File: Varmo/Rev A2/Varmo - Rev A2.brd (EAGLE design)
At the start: 131 x 87 mm, 88 parts, among them J1 22-05-7028-02, J2 22-05-7028-02, J3 22-05-7038-03, J4 22-05-7038-03, J5 22-05-7038-03, J6 22-05-7038-03, J7 22-05-7028-02, J8 22-05-7028-02, J9 22-05-7038-03, T1 MMBT2222AL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

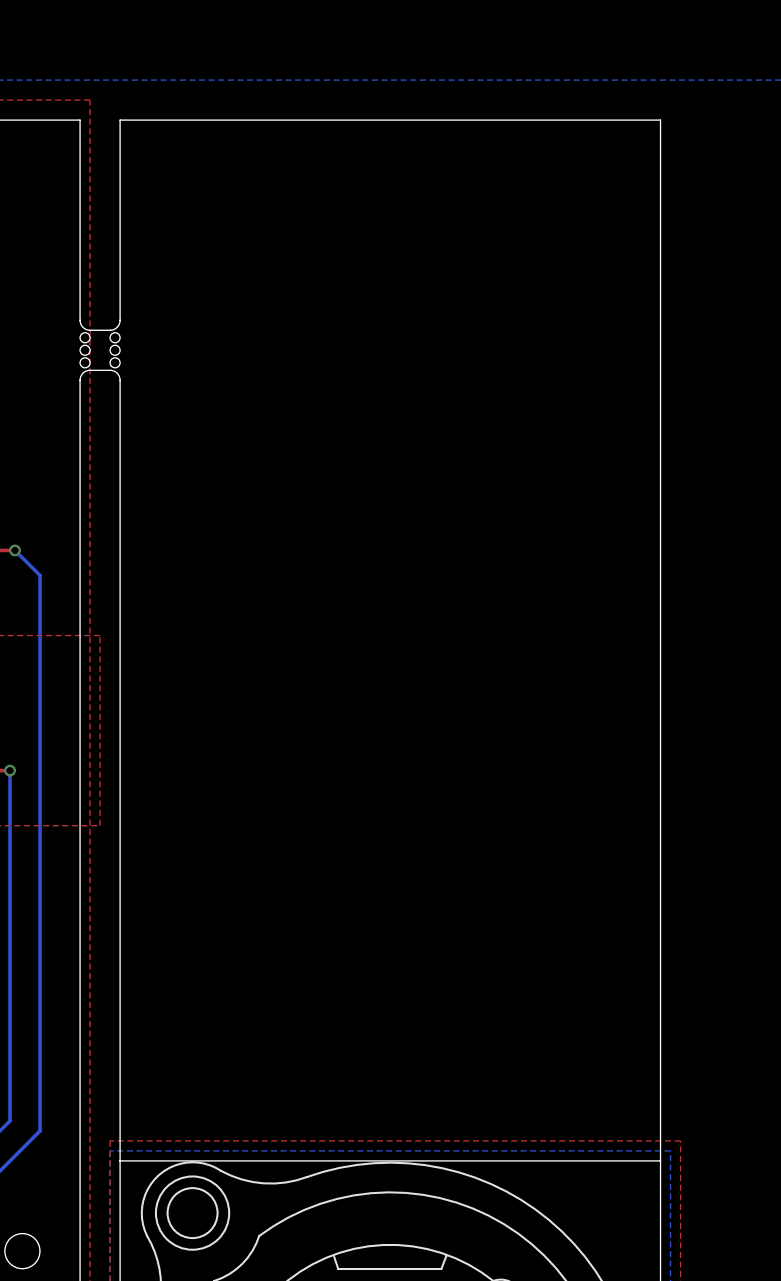
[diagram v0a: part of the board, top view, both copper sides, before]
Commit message: Add joystick to the board varmo rev a2
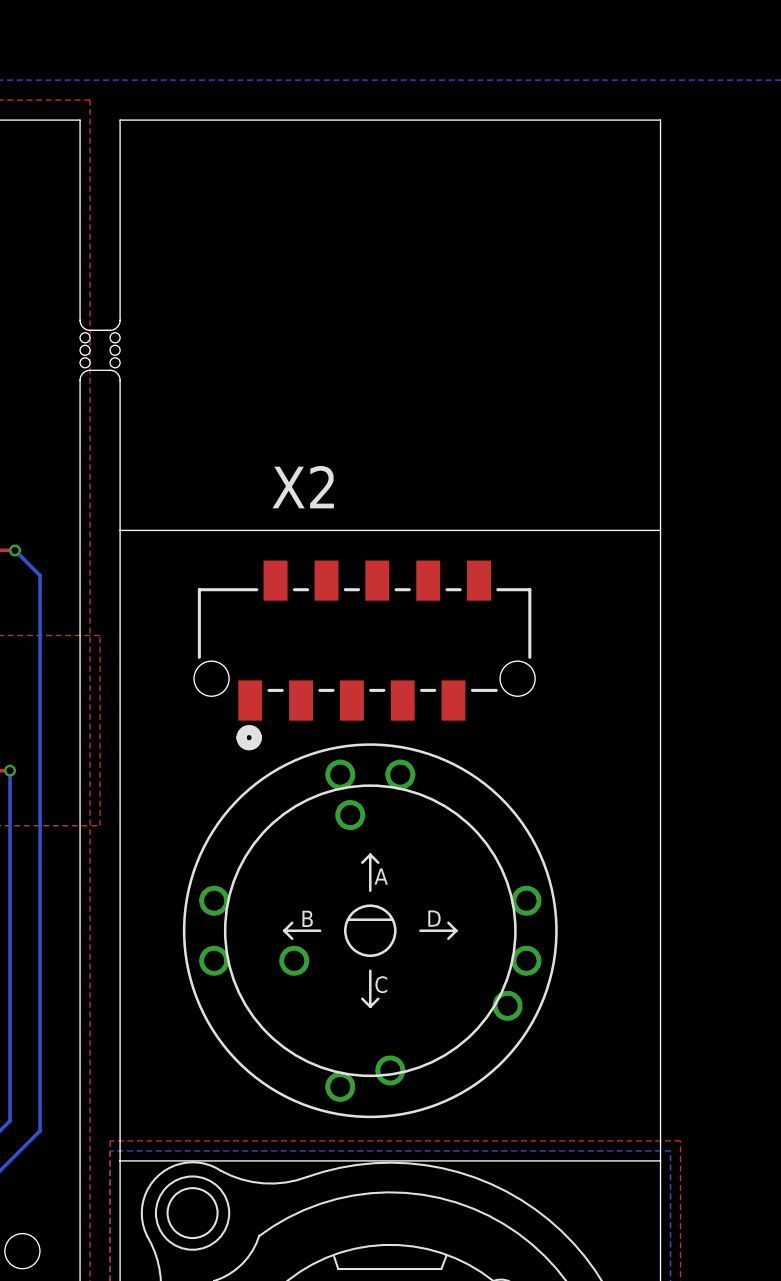
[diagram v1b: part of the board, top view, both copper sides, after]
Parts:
- added ENC1: RKJXTF42001, encoder:RKJXT1F
- added X2: 90814-0210, Molex_By_element14_Batch_1:MOLEX_90814-0210
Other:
- outline, holes or cut-outs redrawn
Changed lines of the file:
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@@
 <hole x="102.25" y="10.125" drill="0.5"/>
 <wire x1="104" y1="11" x2="104" y2="35" width="0" layer="20"/>
-<wire x1="104" y1="35" x2="104" y2="74" width="0" layer="20"/>
+<wire x1="104" y1="35" x2="104" y2="66.5" width="0" layer="20"/>
+<wire x1="104" y1="66.5" x2="104" y2="74" width="0" layer="20"/>
 <wire x1="104" y1="74" x2="103.5" y2="74.5" width="0" layer="20" curve="90"/>
 <wire x1="103.5" y1="74.5" x2="102.5" y2="74.5" width="0" layer="20"/>
@@
 <hole x="102.25" y="27" drill="0.5"/>
 <hole x="102.25" y="27.625" drill="0.5"/>
-<wire x1="131" y1="35" x2="131" y2="87" width="0" layer="20"/>
+<wire x1="131" y1="35" x2="131" y2="66.5" width="0" layer="20"/>
+<wire x1="131" y1="66.5" x2="131" y2="87" width="0" layer="20"/>
+<wire x1="104" y1="66.5" x2="131" y2="66.5" width="0" layer="20"/>
 </plain>
 <attributes>
@@
 </element>
 <element name="U$1" library="cc-by-sa" package="CC-BY-NC-SA" value="CC-BY-NC-SA" x="51.5" y="32.5" rot="R270"/>
+<element name="ENC1" library="encoder" package="RKJXT1F" value="RKJXTF42001" x="116.5" y="46.5"/>
+<element name="X2" library="Molex_By_element14_Batch_1" package="MOLEX_90814-0210" value="90814-0210" x="110.5" y="58">
+<attribute name="MF" value="" x="110.5" y="58" size="1.778" layer="27" display="off"/>
+<attribute name="OC_NEWARK" value="34R6217" x="110.5" y="58" size="1.778" layer="27" display="off"/>
+<attribute name="PACKAGE" value="CONN-10POS" x="110.5" y="58" size="1.778" layer="27" display="off"/>
+<attribute name="MPN" value="90814-0210" x="110.5" y="58" size="1.778" layer="27" display="off"/>
+<attribute name="SUPPLIER" value="Molex" x="110.5" y="58" size="1.778" layer="27" display="off"/>
+<attribute name="OC_FARNELL" value="1757026" x="110.5" y="58" size="1.778" layer="27" display="off"/>
+</element>
 </elements>
 <signals>

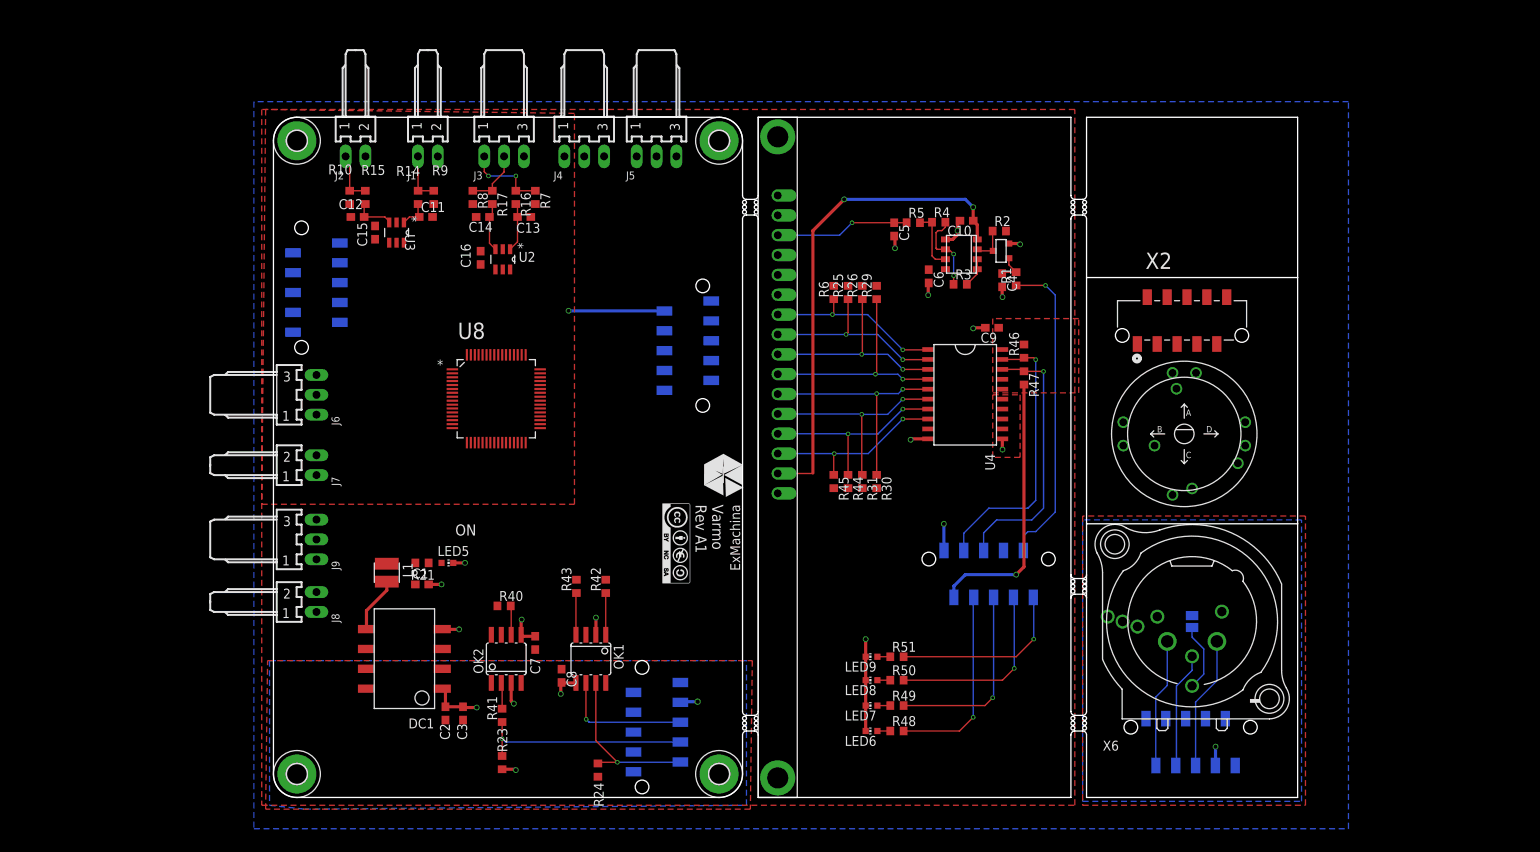
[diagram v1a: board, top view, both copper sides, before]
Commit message: Place the component and route the joystick panel
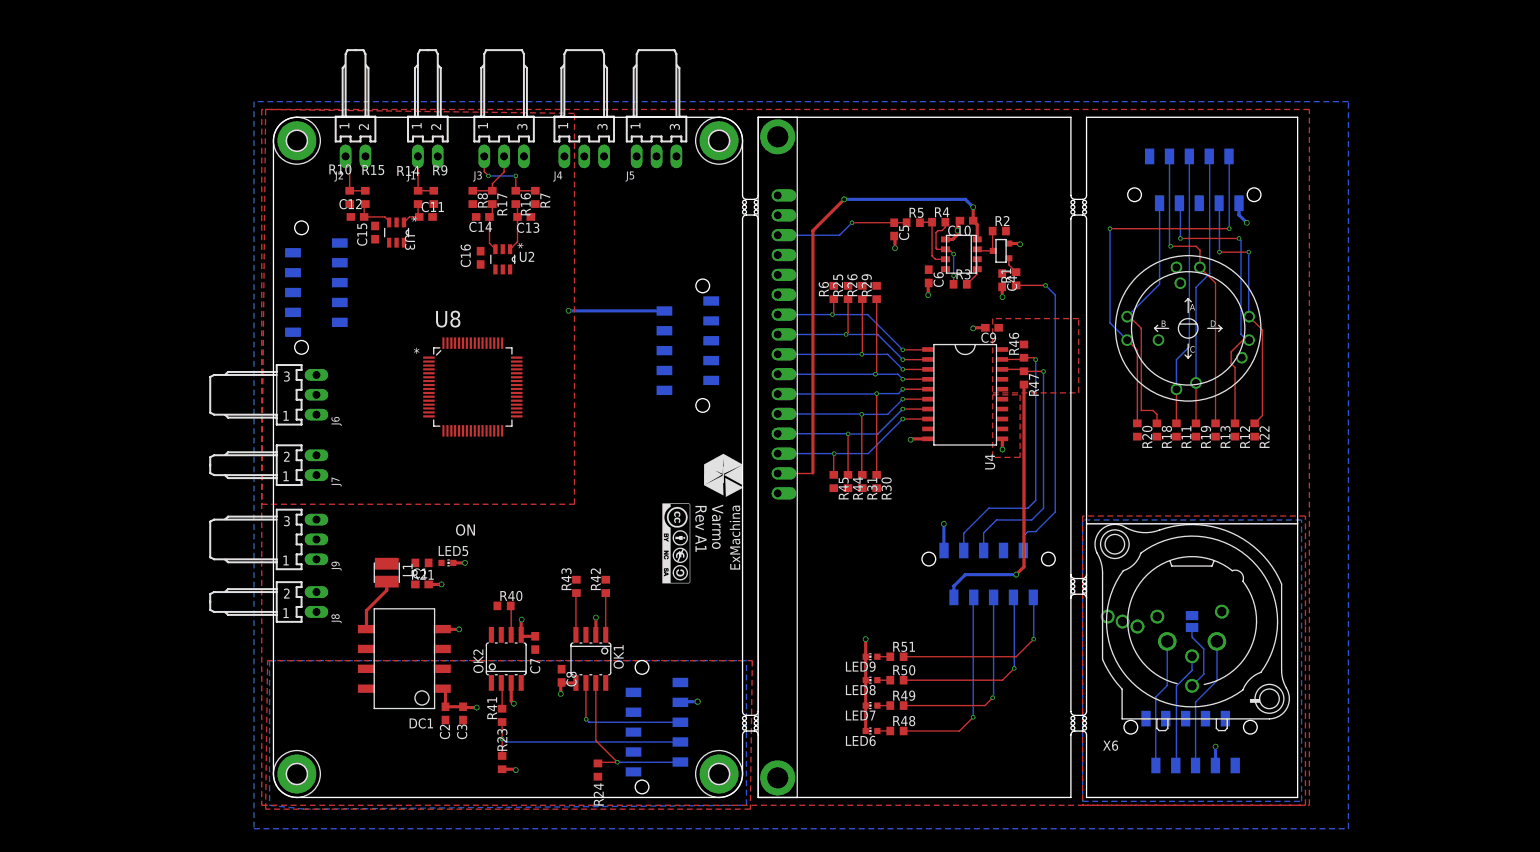
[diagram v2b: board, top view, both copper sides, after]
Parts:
- added R11, R12, R13, R18, R19, R20, R22: 4k7, rcl:R0603
- moved X2 22.2 mm to (123.5, 76.0), flipped to the bottom
- moved ENC1 13.5 mm to (117.0, 60.0)
- moved U8 3.35 mm to (25.5, 52.5)
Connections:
- new net DIR_A: ENC1.A, R11.1, X1.6, X2.6
- new net DIR_B: ENC1.B, R12.1, X1.7, X2.7
- new net DIR_C: ENC1.C, R13.1, X1.8, X2.8
- new net DIR_D: ENC1.D, R18.1, X1.9, X2.9
- new net ENCODER_A: ENC1.ENCODERA, R20.1, X1.2, X2.2
- new net ENCODER_B: ENC1.ENCODERB, R22.1, X1.3, X2.3
- new net N$40: ENC1.COM
- new net PUSH: ENC1.PUSH, R19.1, X1.4, X2.4
- net +5V/1: now also R11.2, R12.2, R13.2, R18.2, R19.2, R20.2, R22.2, X1.1, X2.1
- net GND1: now also ENC1.ENCODERCOM, X1.10, X1.5, X2.10, X2.5
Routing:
- net ENCODER_A: track 0.00 -> 50.9 mm, vias 0 -> 2
- net DIR_C: track 0.00 -> 38.5 mm, vias 0 -> 1
- net DIR_B: track 0.00 -> 38.0 mm, vias 0 -> 2
- net PUSH: track 0.00 -> 34.9 mm
- net DIR_A: track 0.00 -> 34.8 mm
- net ENCODER_B: track 0.00 -> 33.1 mm, vias 0 -> 2
- net DIR_D: track 0.00 -> 32.5 mm
- net +5V/1: track 3.42 -> 6.33 mm, vias 1 -> 2
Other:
- outline, holes or cut-outs redrawn

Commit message: Route the LCD panel with the good placement for the four LED Route the joystick panel with the mounting hole
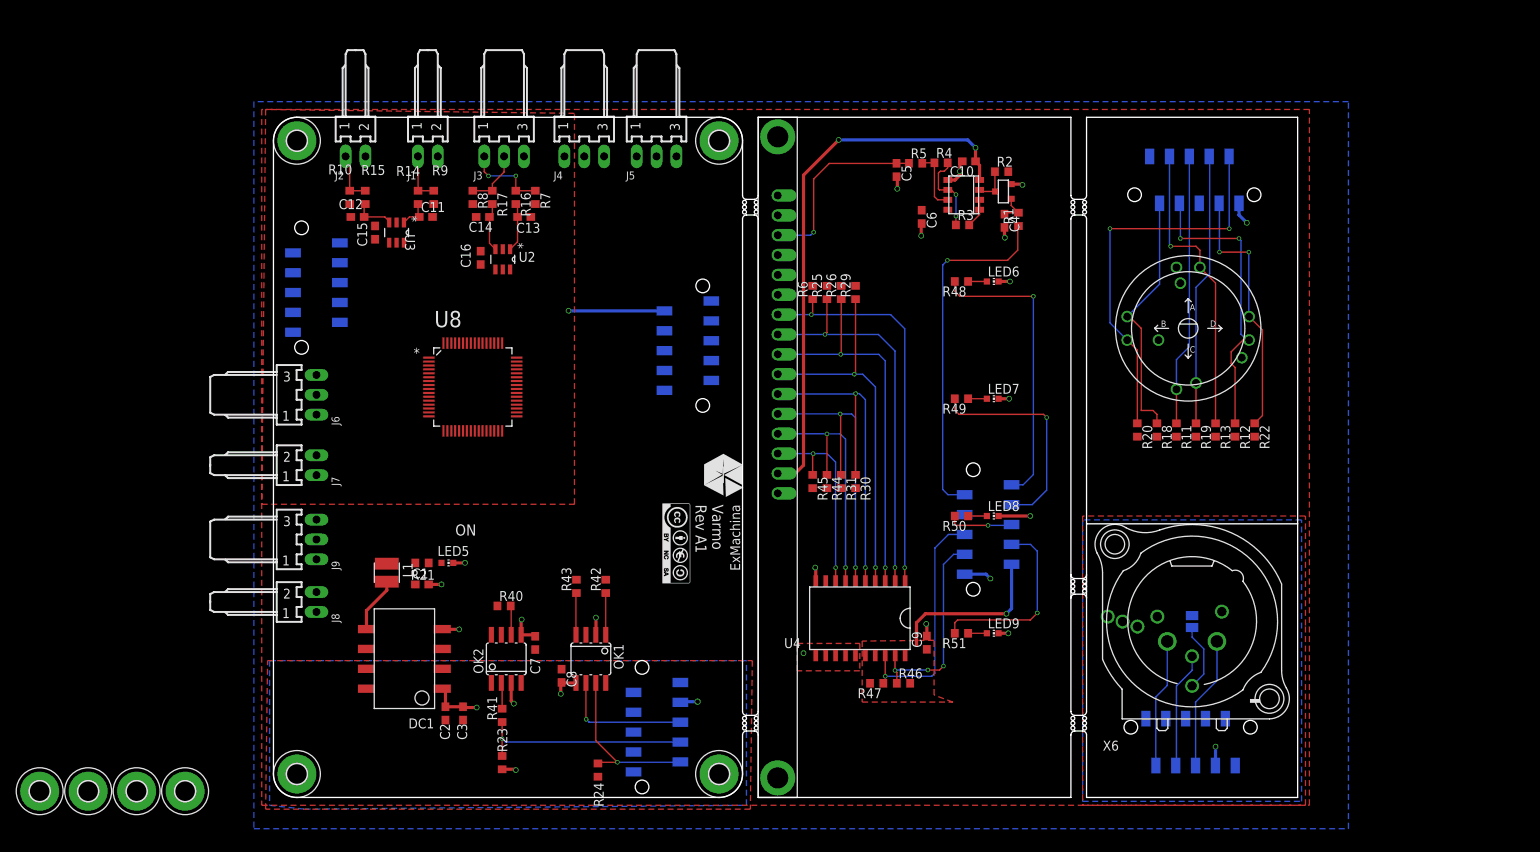
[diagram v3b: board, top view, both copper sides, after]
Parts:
- added MP5, MP6, MP7, MP8: MOUNT-PAD2.5, holes:P2.5
- moved LED6 59.6 mm to (92.0, 66.0), turned to 270 degrees
- moved R48 58.1 mm to (88.0, 66.0), turned to 180 degrees
- moved R46 45.2 mm to (80.6, 14.6), turned to 0 degrees
- moved R47 43.4 mm to (77.2, 14.6), turned to 180 degrees
- moved LED7 42.2 mm to (92.0, 51.0), turned to 270 degrees
- moved C9 41.1 mm to (83.6, 19.8), turned to 90 degrees
- moved R49 40.1 mm to (88.0, 51.0), turned to 180 degrees
- moved U4 31.6 mm to (75.1, 22.9), turned to 180 degrees
- moved LED8 26.1 mm to (92.0, 36.0), turned to 270 degrees
- moved R50 22.6 mm to (88.0, 36.0), turned to 180 degrees
- moved LED9 15.8 mm to (92.0, 21.0), turned to 270 degrees
- moved R51 8.78 mm to (88.0, 21.0), turned to 180 degrees
- moved C6 7.65 mm to (82.9, 74.3)
- moved C4 7.61 mm to (93.5, 73.8)
- moved C5 7.61 mm to (79.7, 80.3)
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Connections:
- net LED_STATUS_1: now also U5.10, U6.10; no longer U5.4, U6.4
- net LED_STATUS_2: now also U5.8, U6.8; no longer U5.6, U6.6
- net LED_STATUS_3: now also U5.6, U6.6; no longer U5.8, U6.8
- net LED_STATUS_4: now also U5.4, U6.4; no longer U5.10, U6.10
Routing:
- net D0: track 23.2 -> 51.3 mm
- net D1: track 25.2 -> 49.9 mm
- net D2: track 27.1 -> 49.4 mm
- net D3: track 29.2 -> 47.7 mm
- net LED_STATUS_3: track 23.9 -> 8.42 mm
- net D4: track 29.9 -> 45.2 mm
- net +3V3: track 47.0 -> 33.7 mm
- net LED_STATUS_1: track 25.0 -> 37.7 mm
- net D5: track 27.8 -> 38.9 mm
- net SDA: track 35.6 -> 26.7 mm, vias 1 -> 3
- net VO: track 17.2 -> 24.6 mm
- net VEE: track 62.4 -> 69.5 mm
- net D6: track 25.8 -> 32.4 mm
- net GND1: track 38.0 -> 32.5 mm, vias 14 -> 17
- net PWM_CONTRASTE: track 40.5 -> 45.3 mm
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
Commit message: Move the link between joystick panel and LCD screen
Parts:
- moved MP8 174.2 mm to (127.6, 75.2)
- moved MP7 156.3 mm to (127.9, 39.0)
- moved MP5 140.2 mm to (107.5, 75.2)
- moved MP6 130.3 mm to (107.1, 39.0)
- moved ENC1 3.63 mm to (117.5, 56.4)
- moved R11 3.60 mm to (115.6, 43.4)
- moved R12 3.60 mm to (123.1, 43.4)
- moved R13 3.60 mm to (120.6, 43.4)
- moved R18 3.60 mm to (113.1, 43.4)
- moved R19 3.60 mm to (118.1, 43.4)
- moved R20 3.60 mm to (110.6, 43.4)
- moved R22 3.60 mm to (125.6, 43.4)
- moved X2 3.00 mm to (123.6, 79.0)
- moved SJ5 1.80 mm to (117.5, 20.7)
- moved X6 1.80 mm to (117.5, 20.7)
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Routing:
- net DIR_B: track 38.0 -> 45.4 mm
- net DIR_A: track 34.8 -> 41.9 mm
- net DIR_C: track 38.5 -> 45.3 mm
- net +5V/1: track 6.43 -> 13.2 mm
- net PUSH: track 34.9 -> 41.7 mm
- net ENCODER_B: track 33.1 -> 39.7 mm
- net DIR_D: track 32.5 -> 37.7 mm
- net ENCODER_A: track 50.9 -> 53.7 mm
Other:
- outline, holes or cut-outs redrawn

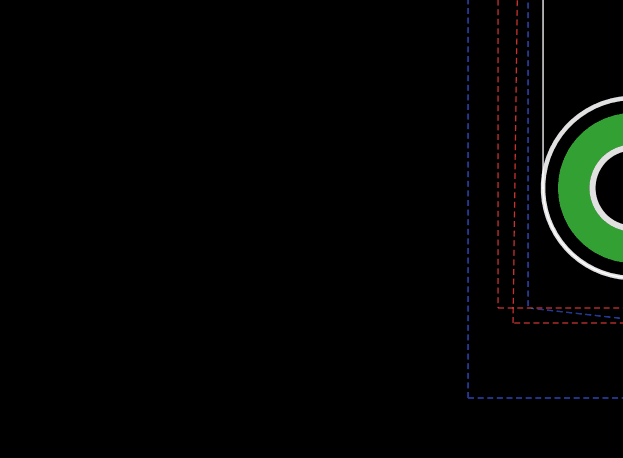
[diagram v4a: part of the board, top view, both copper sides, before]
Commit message: Add the clocks to the arm
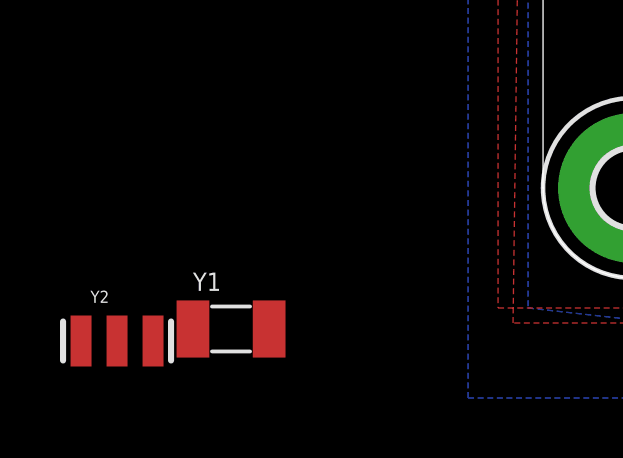
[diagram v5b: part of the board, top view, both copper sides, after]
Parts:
- added Y1: 32.768kHz, 12.5pF, crystal:ABS07
- added Y2: 8MHz, resonator:RESONATOR-SMD
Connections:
- new net N$15: U8.19, Y1.2
- new net N$16: U8.20, Y1.1
- new net N$30: U8.33, Y2.3
- new net N$31: U8.32, Y2.1
- net GND1: now also Y2.2
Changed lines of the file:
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@@
 <element name="MP7" library="holes" package="P2.5" value="MOUNT-PAD2.5" x="127.9" y="39"/>
 <element name="MP8" library="holes" package="P2.5" value="MOUNT-PAD2.5" x="127.6" y="75.2"/>
+<element name="Y1" library="crystal" package="ABS07" value="32.768kHz, 12.5pF" x="-10.4" y="-1.7">
+<attribute name="OC_FARNELL" value="2101347" x="-10.4" y="-1.7" size="1.778" layer="27" display="off"/>
+</element>
+<element name="Y2" library="resonator" package="RESONATOR-SMD" value="8MHz" x="-14.2" y="-2.1"/>
 </elements>
 <signals>
@@
 <via x="94.2" y="66" extent="1-16" drill="0.5"/>
 <via x="94.1" y="51" extent="1-16" drill="0.5"/>
+<contactref element="Y2" pad="2"/>
 <wire x1="29.33" y1="70.1254" x2="32.92" y2="74.25" width="0" layer="19" extent="1-1"/>
 <wire x1="26.5" y1="69.87" x2="29.33" y2="70.1254" width="0" layer="19" extent="1-1"/>
@@
 <wire x1="64.5" y1="66.84" x2="56" y2="55.88" width="0" layer="19" extent="16-16"/>
 <wire x1="112.17" y1="84.9944" x2="95.8" y2="78.35" width="0" layer="19" extent="16-16"/>
+<wire x1="-14.2" y1="-2.1" x2="21.6" y2="21.535" width="0" layer="19" extent="1-1"/>
 </signal>
 <signal name="+5V/1">
@@
 <contactref element="ENC1" pad="COM"/>
 </signal>
+<signal name="N$15">
+<contactref element="U8" pad="19"/>
+<contactref element="Y1" pad="2"/>
+<wire x1="-9.13" y1="-1.7" x2="22.7568" y2="46.8866" width="0" layer="19" extent="1-1"/>
+</signal>
+<signal name="N$16">
+<contactref element="Y1" pad="1"/>
+<contactref element="U8" pad="20"/>
+<wire x1="-11.67" y1="-1.7" x2="23.2394" y2="46.8866" width="0" layer="19" extent="1-1"/>
+</signal>
+<signal name="N$30">
+<contactref element="Y2" pad="3"/>
+<contactref element="U8" pad="33"/>
+<wire x1="-13" y1="-2.1" x2="31.1134" y2="48.7408" width="0" layer="19" extent="1-1"/>
+</signal>
+<signal name="N$31">
+<contactref element="U8" pad="32"/>
+<contactref element="Y2" pad="1"/>
+<wire x1="-15.4" y1="-2.1" x2="29.2592" y2="46.8866" width="0" layer="19" extent="1-1"/>
+</signal>
 </signals>
